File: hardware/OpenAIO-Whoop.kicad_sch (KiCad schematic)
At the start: 0 parts

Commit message: schematic: P4 contract, root sheet and empty sub-sheets (10 sheets, 268 refs mapped)
Co-Authored-By: Claude Opus 5.5 <noreply@anthropic.com>
Claude-Session: https://claude.ai/code/session_01RFaS5jnC9tnPam9GBgmGnG
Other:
- added sheet BLACKBOX (blackbox.kicad_sch)
- added sheet ESC1 (esc_channel.kicad_sch)
- added sheet ESC2 (esc_channel.kicad_sch)
- added sheet ESC3 (esc_channel.kicad_sch)
- added sheet ESC4 (esc_channel.kicad_sch)
- added sheet IMU (imu.kicad_sch)
- added sheet LED (led.kicad_sch)
- added sheet OSD (osd.kicad_sch)
- added sheet PADS (pads.kicad_sch)
- added sheet POWER (power.kicad_sch)
- added sheet RP2350A (rp2350a.kicad_sch)
- added sheet RX (rx_esp32_sx1281.kicad_sch)
- added sheet VTX (vtx.kicad_sch)
- note added: "16 MB NOR PY25Q128HA"
- note added: "BATTERY MOTOR LANDS USER UART LED / BUZZER CAMERA HD (O4) USB JST SH"
- note added: "BMI270 1V8 LDO"
- note added: "EFM8BB51 BLUEJAY BB51 A 3x AGM210MAP"
- note added: "ESP32-PICO-V3 SX1281 + TCXO LPF + WIRE ANT WIFI CHIP ANT BOOT BUTTON"
- note added: "PIO OSD SYNC + CLAMP LEVEL SWITCH"
- note added: "POWER TABLE"
- note added: "RP2354A CORE SMPS 1V1 12 MHz XTAL USB 27R VBAT + CURR ADC BEEPER FET BOOT + SWD VIAS"
- note added: "RTC6705 SE5004L PA PNP DRIVE 3V3_VTX LDO HD GATE"
- note added: "STATUS LEDS"
- note added: "TVS + SHUNT INA186 CURRENT 5V BOOST USB OVP 5V MUX 3V3 LDO CAM 5V FILTER O4 HD SWITCH ESC3 BULK"
- company: OpenDrone -> (none)
- title: OpenAIO-Whoop -> OpenAIO-Whoop overview (1S whoop AIO)

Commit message: schematic: integrated (ERC 0 errors / 2 justified warnings; check_netlist 7/7; conventions 0 FAIL; visual 0 hits; 268/268 refs match bom_plan; FC+RX pin maps match PINMAP)
Co-Authored-By: Claude Opus 5.5 <noreply@anthropic.com>
Claude-Session: https://claude.ai/code/session_01RFaS5jnC9tnPam9GBgmGnG
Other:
- sheet RX ports: added VTX_AMP_PWM; removed PA_BIAS_PWM
- sheet VTX ports: added VTX_AMP_PWM; removed PA_BIAS_PWM
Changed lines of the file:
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@@
 				)
 			)
-			(table_cell "1.82 A at 3.0 V in"
+			(table_cell "0.70 A analog / 1.48 A HD (BEC 1.5 A cont.)"
 				(exclude_from_sim no)
 				(at 119.38 231.14 0)
@@
 				)
 			)
-			(table_cell "0.70 A analog, 1.48 A HD"
+			(table_cell "0.70 A analog, about 0.25 A HD"
 				(exclude_from_sim no)
 				(at 119.38 234.95 0)
@@
 				)
 			)
-			(table_cell "0.10 A"
+			(table_cell "0.10 A typ, about 0.17 A at max PA"
 				(exclude_from_sim no)
 				(at 119.38 250.19 0)
@@
 		)
 	)
-	(label "PA_BIAS_PWM"
+	(label "VTX_AMP_PWM"
 		(at 276.86 43.18 0)
 		(effects
@@
 			)
 		)
-		(pin "PA_BIAS_PWM" input
+		(pin "VTX_AMP_PWM" input
 			(at 297.18 43.18 180)
 			(effects
@@
 			)
 		)
-		(pin "PA_BIAS_PWM" output
+		(pin "VTX_AMP_PWM" output
 			(at 274.32 43.18 0)
 			(effects

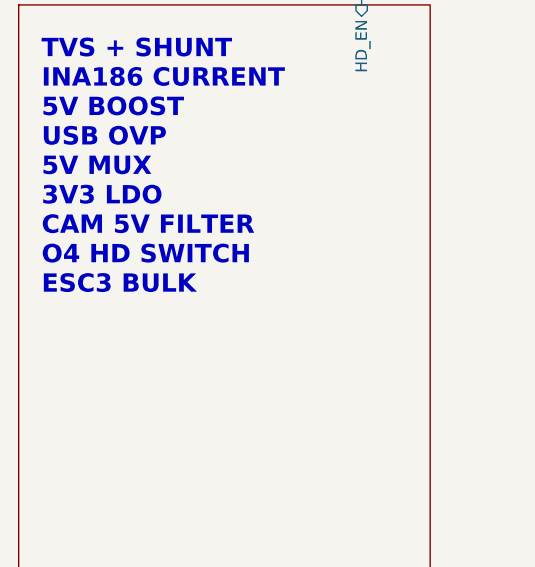
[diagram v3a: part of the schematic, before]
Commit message: hardware: floorplan v3 review pass (RX RF corner blocker fixed; majors listed in FLOORPLAN.md Open)
Co-Authored-By: Claude Opus 5.5 <noreply@anthropic.com>
Claude-Session: https://claude.ai/code/session_01RFaS5jnC9tnPam9GBgmGnG
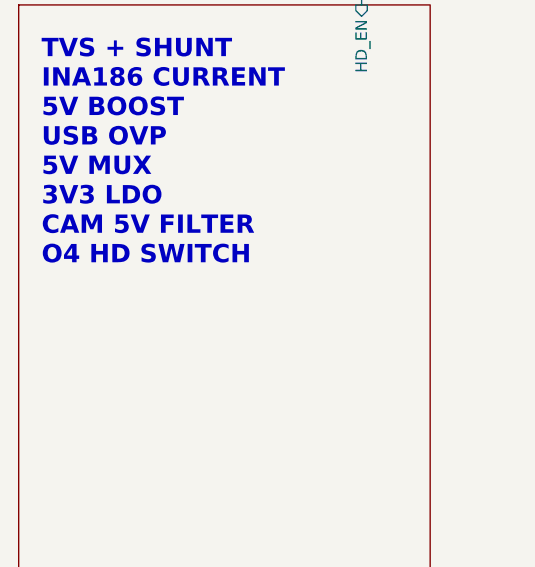
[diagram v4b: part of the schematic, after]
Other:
- note added: "TVS + SHUNT INA186 CURRENT 5V BOOST USB OVP 5V MUX 3V3 LDO CAM 5V FILTER O4 HD SWITCH"
- note removed: "TVS + SHUNT INA186 CURRENT 5V BOOST USB OVP 5V MUX 3V3 LDO CAM 5V FILTER O4 HD SWITCH ESC3 BULK"
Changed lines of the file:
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@@
 		)
 	)
-	(text "TVS + SHUNT\nINA186 CURRENT\n5V BOOST\nUSB OVP\n5V MUX\n3V3 LDO\nCAM 5V FILTER\nO4 HD SWITCH\nESC3 BULK"
+	(text "TVS + SHUNT\nINA186 CURRENT\n5V BOOST\nUSB OVP\n5V MUX\n3V3 LDO\nCAM 5V FILTER\nO4 HD SWITCH"
 		(exclude_from_sim no)
 		(at 20.32 34.29 0)

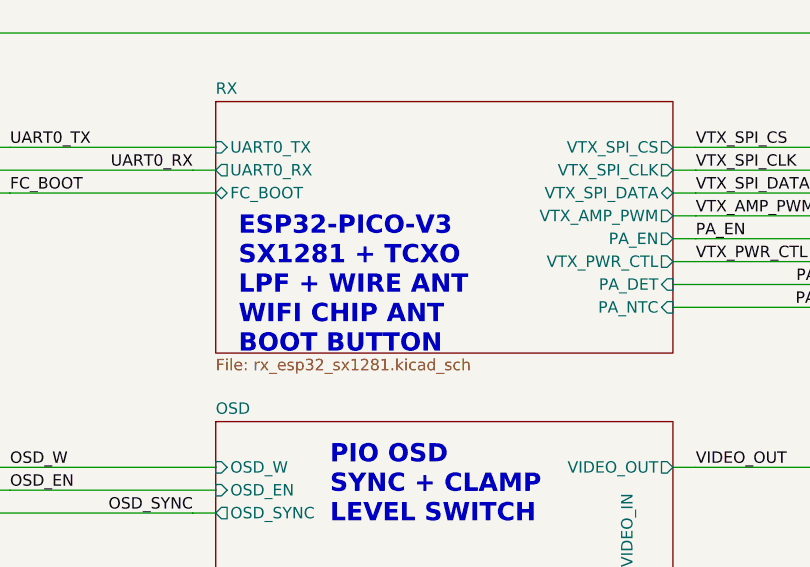
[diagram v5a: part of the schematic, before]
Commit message: schematic: review complete (4 rounds; U20 pin 1 to GND, footprint filters fixed, TPS22810DRVR, R54 270R); ERC 0 errors, check_netlist 7/7; D85-D87
Co-Authored-By: Claude Opus 5.5 <noreply@anthropic.com>
Claude-Session: https://claude.ai/code/session_01RFaS5jnC9tnPam9GBgmGnG
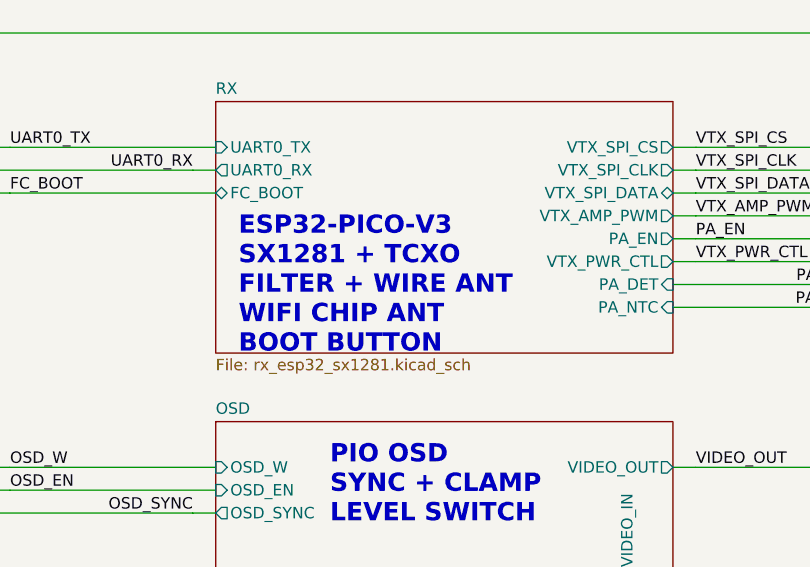
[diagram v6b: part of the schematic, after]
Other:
- note added: "ESP32-PICO-V3 SX1281 + TCXO FILTER + WIRE ANT WIFI CHIP ANT BOOT BUTTON"
- note removed: "ESP32-PICO-V3 SX1281 + TCXO LPF + WIRE ANT WIFI CHIP ANT BOOT BUTTON"
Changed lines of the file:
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@@
 		)
 	)
-	(text "ESP32-PICO-V3\nSX1281 + TCXO\nLPF + WIRE ANT\nWIFI CHIP ANT\nBOOT BUTTON"
+	(text "ESP32-PICO-V3\nSX1281 + TCXO\nFILTER + WIRE ANT\nWIFI CHIP ANT\nBOOT BUTTON"
 		(exclude_from_sim no)
 		(at 226.06 43.18 0)

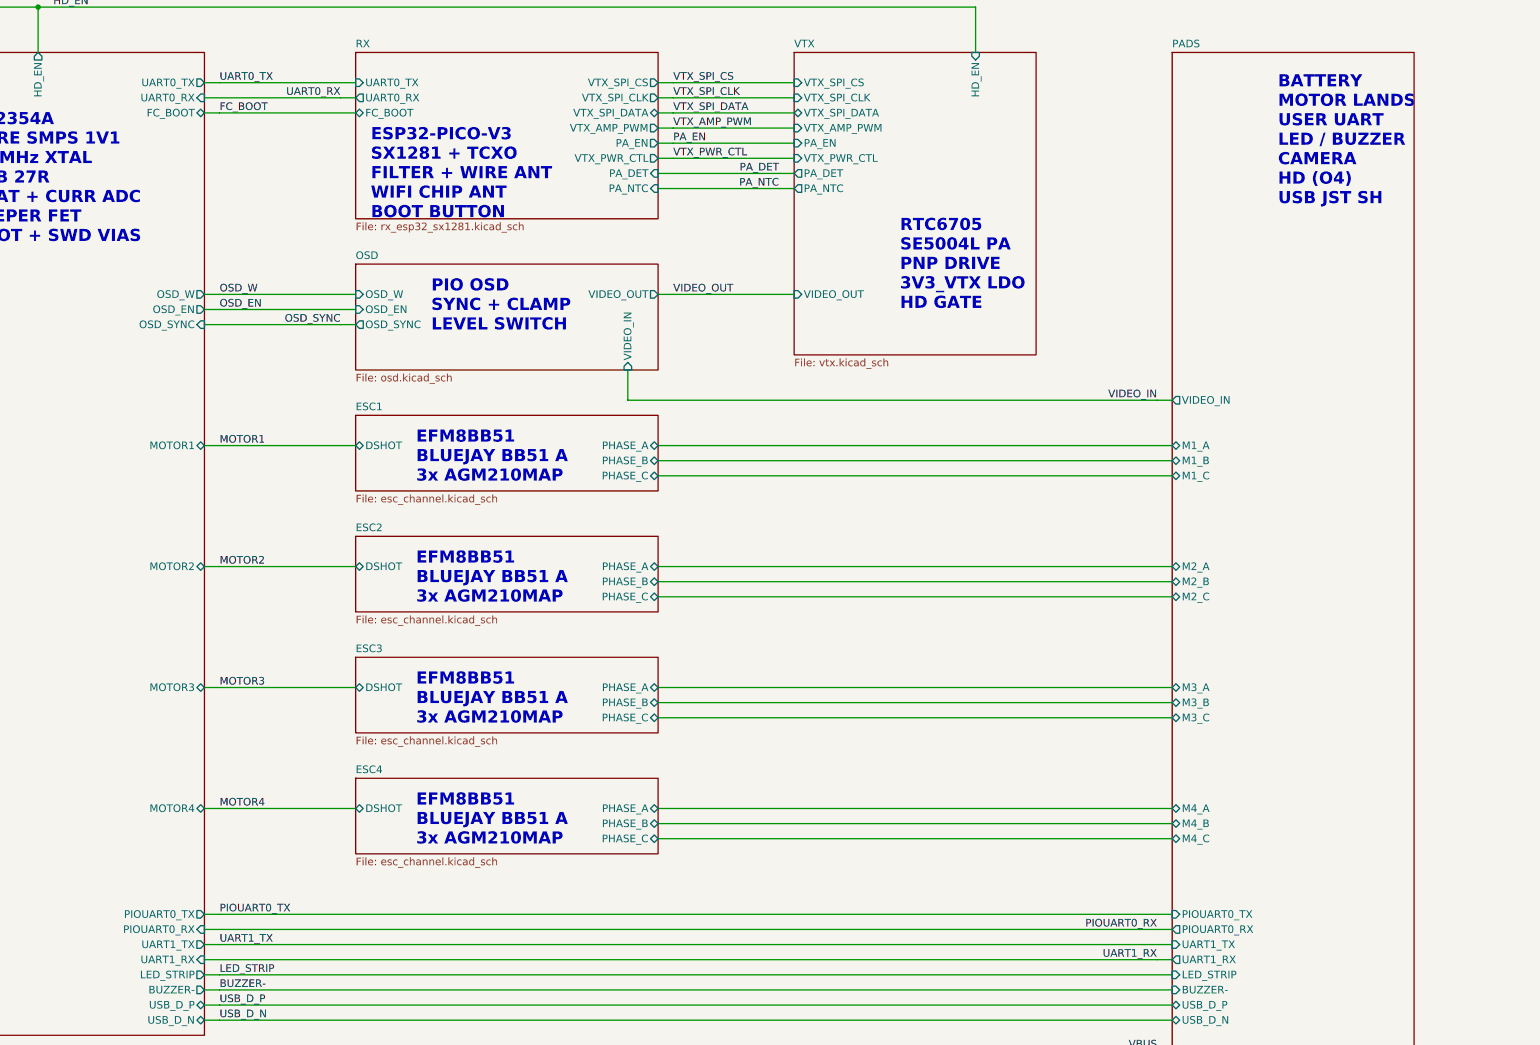
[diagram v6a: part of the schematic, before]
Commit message: wip: v4 prep in progress (D89 UART pad removal, D93 3D model fixes, Wi-Fi antenna research)
Snapshot of running workflows; final numbers follow when each verifies.

Co-Authored-By: Claude Opus 5.5 <noreply@anthropic.com>
Claude-Session: https://claude.ai/code/session_01RFaS5jnC9tnPam9GBgmGnG
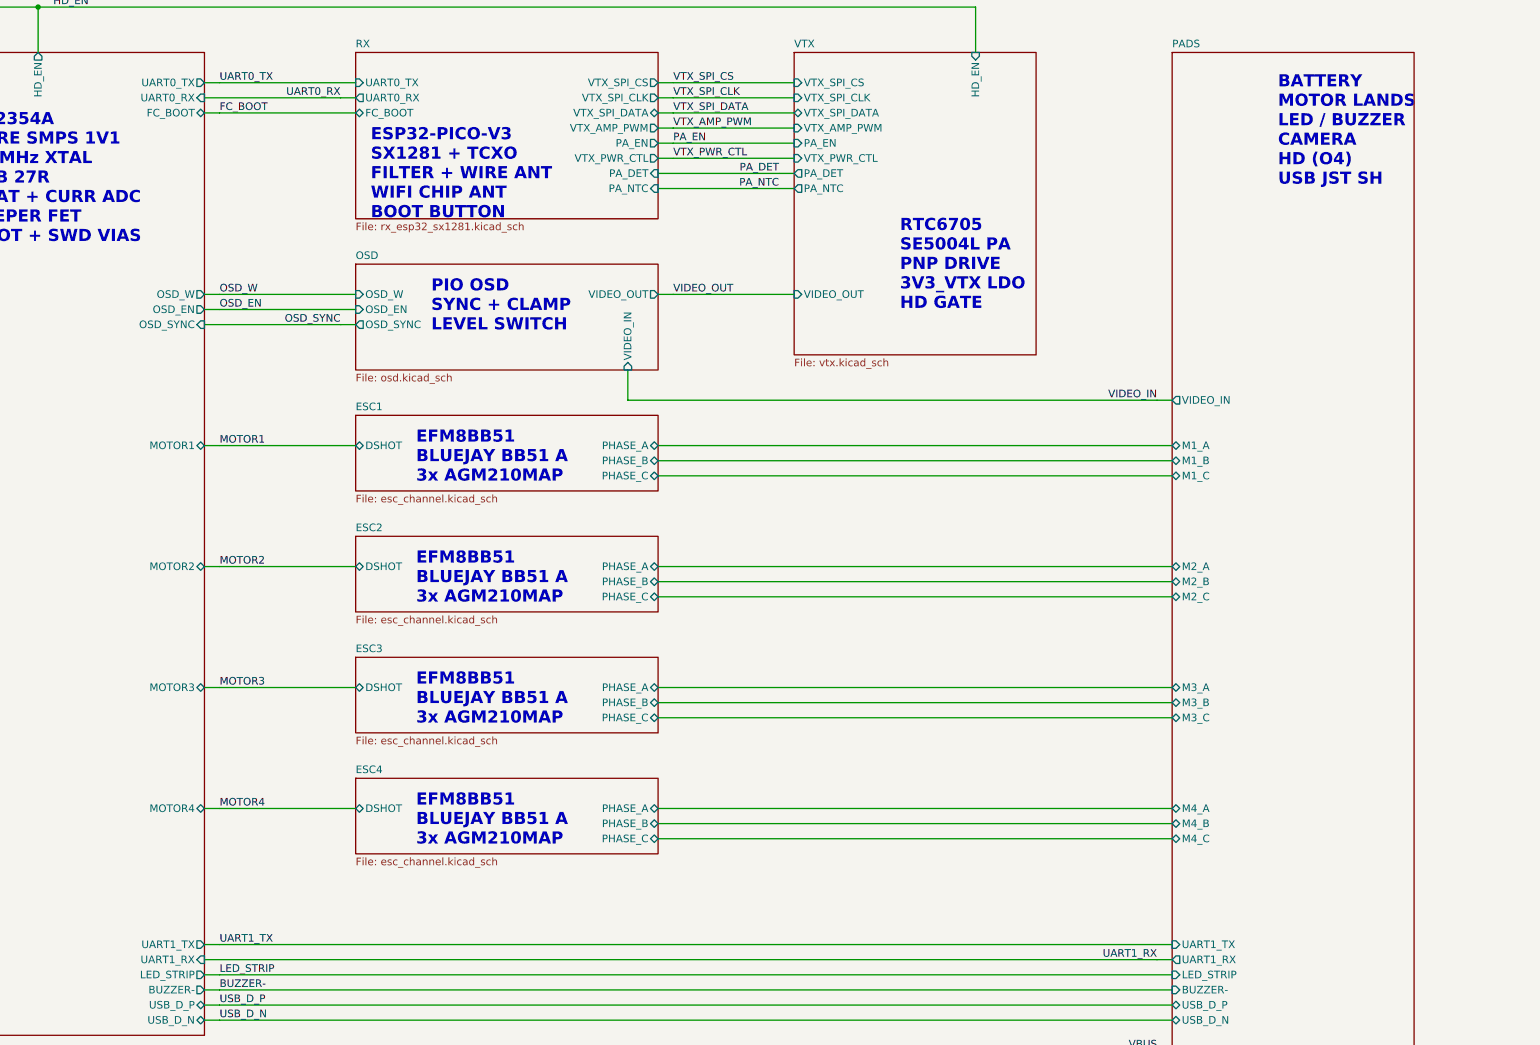
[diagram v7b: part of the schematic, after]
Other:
- sheet PADS ports: added none; removed PIOUART0_RX, PIOUART0_TX
- sheet RP2350A ports: added none; removed PIOUART0_RX, PIOUART0_TX
- note added: "BATTERY MOTOR LANDS LED / BUZZER CAMERA HD (O4) USB JST SH"
- note removed: "BATTERY MOTOR LANDS USER UART LED / BUZZER CAMERA HD (O4) USB JST SH"
